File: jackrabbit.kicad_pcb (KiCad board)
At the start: 2 copper layers, 50 x 48.3 mm, 61 parts, among them J1 USB_C, J2 PinHeader_2.54mm_02x08, J3 PinHeader_2.54mm_02x08, J4 PinHeader_2.54mm_02x04, J5 PinHeader_2.54mm_02x04, J6 PinHeader_2.54mm_01x04, J7 PinHeader_2.54mm_01x03, SW1 SW_Push, SW2 SW_Push, U1 MIC5319-3.3YD5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

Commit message: Add pullups to disable buffers on power-on
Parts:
- added R18: 10k, Resistor_SMD:R_0603_1608Metric_Pad0.98x0.95mm_HandSolder, F.Cu at (115.6, 94.0)
- added R19: 10k, Resistor_SMD:R_0603_1608Metric_Pad0.98x0.95mm_HandSolder, F.Cu at (115.6, 96.5)
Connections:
- U2 pad 19: GND -> /~{OE_A}
- U4 pad 31: unconnected-(U4-Pad31) -> /~{OE_A}
- U4 pad 32: unconnected-(U4-Pad32) -> /~{OE_B}
- U5 pad 19: GND -> /~{OE_B}
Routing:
- net /QSPI_SD3: track 20.6 -> 22.2 mm
- net /QSPI_SD1: track 8.21 -> 6.62 mm
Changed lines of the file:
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@@
   (title_block
     (title "Jackrabbit RP2040 Logic Analyzer")
-    (date "2022-07-10")
+    (date "2022-07-21")
     (rev "A")
     (comment 2 "Ray Sun")
@@
   (net 74 "/DIG14")
   (net 75 "/DIG15")
-  (net 76 "unconnected-(U4-Pad32)")
+  (net 76 "/~{OE_A}")
   (net 77 "unconnected-(U4-Pad34)")
-  (net 78 "unconnected-(U4-Pad31)")
+  (net 78 "/~{OE_B}")
   (net 79 "Net-(R7-Pad1)")
   (net 80 "Net-(R8-Pad1)")
@@
       (net 80 "Net-(R8-Pad1)") (pinfunction "GPIO19") (pintype "bidirectional"))
     (pad "31" smd roundrect (at 3.65 1.8 315) (size 1.3 0.2) (layers "F.Cu" "F.Paste" "F.Mask") (roundrect_rratio 0.25)
-      (net 78 "unconnected-(U4-Pad31)") (pinfunction "GPIO20") (pintype "bidirectional+no_connect"))
+      (net 76 "/~{OE_A}") (pinfunction "GPIO20") (pintype "bidirectional"))
     (pad "32" smd roundrect (at 3.65 1.4 315) (size 1.3 0.2) (layers "F.Cu" "F.Paste" "F.Mask") (roundrect_rratio 0.25)
-      (net 76 "unconnected-(U4-Pad32)") (pinfunction "GPIO21") (pintype "bidirectional+no_connect"))
+      (net 78 "/~{OE_B}") (pinfunction "GPIO21") (pintype "bidirectional"))
     (pad "33" smd roundrect (at 3.65 1 315) (size 1.3 0.2) (layers "F.Cu" "F.Paste" "F.Mask") (roundrect_rratio 0.25)
       (net 1 "+3V3") (pinfunction "IOVDD") (pintype "power_in"))
@@
       (net 89 "Net-(RN2-Pad1)") (pinfunction "B0") (pintype "tri_state"))
     (pad "19" smd roundrect (at 2.8625 -1.75 90) (size 1.475 0.3) (layers "F.Cu" "F.Paste" "F.Mask") (roundrect_rratio 0.25)
-      (net 2 "GND") (pinfunction "CE") (pintype "input"))
+      (net 78 "/~{OE_B}") (pinfunction "CE") (pintype "input"))
     (pad "20" smd roundrect (at 2.8625 -2.25 90) (size 1.475 0.3) (layers "F.Cu" "F.Paste" "F.Mask") (roundrect_rratio 0.25)
       (net 1 "+3V3") (pinfunction "VCC") (pintype "power_in"))
@@
     )
   )
+  (footprint "Resistor_SMD:R_0603_1608Metric_Pad0.98x0.95mm_HandSolder" (layer "F.Cu")
+    (at 115.632 96.475)
+    (descr "Resistor SMD 0603 (1608 Metric), square (rectangular) end terminal, IPC_7351 nominal with elongated pad for handsoldering. (Body size source: IPC-SM-782 page 72, https://www.pcb-3d.com/wordpress/wp-content/uploads/ipc-sm-782a_amendment_1_and_2.pdf), generated with kicad-footprint-generator")
+    (tags "resistor handsolder")
+    (property "Sheetfile" "jackrabbit.kicad_sch")
+    (property "Sheetname" "")
+    (attr smd)
+    (fp_text reference "R19" (at 0 -1.429992 unlocked) (layer "F.SilkS") hide
+      (effects (font (size 0.762 0.762) (thickness 0.127)))
+    )
+    (fp_text value "10k" (at 0 1.43 unlocked) (layer "F.Fab")
+      (effects (font (size 0.762 0.762) (thickness 0.127)))
+    )
+    (fp_text user "${REFERENCE}" (at 0 0 unlocked) (layer "F.Fab")
+      (effects (font (size 0.762 0.762) (thickness 0.127)))
+    )
+    (fp_line (start -0.254724 -0.5225) (end 0.254724 -0.5225) (layer "F.SilkS") (width 0.12))
+    (fp_line (start -0.254724 0.5225) (end 0.254724 0.5225) (layer "F.SilkS") (width 0.12))
+    (fp_line (start -1.65 0.73) (end -1.65 -0.73) (layer "F.CrtYd") (width 0.05))
+    (fp_line (start 1.65 0.73) (end -1.65 0.73) (layer "F.CrtYd") (width 0.05))
+    (fp_line (start 1.65 -0.73) (end 1.65 0.73) (layer "F.CrtYd") (width 0.05))
+    (fp_line (start -1.65 -0.73) (end 1.65 -0.73) (layer "F.CrtYd") (width 0.05))
+    (fp_line (start 0.8 0.4125) (end -0.8 0.4125) (layer "F.Fab") (width 0.1))
+    (fp_line (start 0.8 -0.4125) (end 0.8 0.4125) (layer "F.Fab") (width 0.1))
+    (fp_line (start -0.8 -0.4125) (end 0.8 -0.4125) (layer "F.Fab") (width 0.1))
+    (fp_line (start -0.8 0.4125) (end -0.8 -0.4125) (layer "F.Fab") (width 0.1))
+    (pad "1" smd roundrect (at -0.9125 0) (size 0.975 0.95) (layers "F.Cu" "F.Paste" "F.Mask") (roundrect_rratio 0.25)
+      (net 1 "+3V3") (pintype "passive"))
+    (pad "2" smd roundrect (at 0.9125 0) (size 0.975 0.95) (layers "F.Cu" "F.Paste" "F.Mask") (roundrect_rratio 0.25)
+      (net 78 "/~{OE_B}") (pintype "passive"))
+    (model "${KICAD6_3DMODEL_DIR}/Resistor_SMD.3dshapes/R_0603_1608Metric.wrl"
+      (offset (xyz 0 0 0))
+      (scale (xyz 1 1 1))
+      (rotate (xyz 0 0 0))
+    )
+  )
   (footprint "Connector_PinHeader_2.54mm:PinHeader_1x04_P2.54mm_Vertical" (layer "F.Cu")
     (at 142.81 140.955 90)
@@
   )
   (footprint "Resistor_SMD:R_0603_1608Metric_Pad0.98x0.95mm_HandSolder" (layer "F.Cu")
+    (at 115.632 93.965)
+    (descr "Resistor SMD 0603 (1608 Metric), square (rectangular) end terminal, IPC_7351 nominal with elongated pad for handsoldering. (Body size source: IPC-SM-782 page 72, https://www.pcb-3d.com/wordpress/wp-content/uploads/ipc-sm-782a_amendment_1_and_2.pdf), generated with kicad-footprint-generator")
+    (tags "resistor handsolder")
+    (property "Sheetfile" "jackrabbit.kicad_sch")
+    (property "Sheetname" "")
+    (attr smd)
+    (fp_text reference "R18" (at 0 -1.429995 unlocked) (layer "F.SilkS") hide
+      (effects (font (size 0.762 0.762) (thickness 0.127)))
+    )
+    (fp_text value "10k" (at 0 1.43 unlocked) (layer "F.Fab")
+      (effects (font (size 0.762 0.762) (thickness 0.127)))
+    )
+    (fp_text user "${REFERENCE}" (at 0 0 unlocked) (layer "F.Fab")
+      (effects (font (size 0.762 0.762) (thickness 0.127)))
+    )
+    (fp_line (start -0.254724 0.5225) (end 0.254724 0.5225) (layer "F.SilkS") (width 0.12))
+    (fp_line (start -0.254724 -0.5225) (end 0.254724 -0.5225) (layer "F.SilkS") (width 0.12))
+    (fp_line (start -1.65 0.73) (end -1.65 -0.73) (layer "F.CrtYd") (width 0.05))
+    (fp_line (start 1.65 -0.73) (end 1.65 0.73) (layer "F.CrtYd") (width 0.05))
+    (fp_line (start 1.65 0.73) (end -1.65 0.73) (layer "F.CrtYd") (width 0.05))
+    (fp_line (start -1.65 -0.73) (end 1.65 -0.73) (layer "F.CrtYd") (width 0.05))
+    (fp_line (start -0.8 -0.4125) (end 0.8 -0.4125) (layer "F.Fab") (width 0.1))
+    (fp_line (start -0.8 0.4125) (end -0.8 -0.4125) (layer "F.Fab") (width 0.1))
+    (fp_line (start 0.8 -0.4125) (end 0.8 0.4125) (layer "F.Fab") (width 0.1))
+    (fp_line (start 0.8 0.4125) (end -0.8 0.4125) (layer "F.Fab") (width 0.1))
+    (pad "1" smd roundrect (at -0.9125 0) (size 0.975 0.95) (layers "F.Cu" "F.Paste" "F.Mask") (roundrect_rratio 0.25)
+      (net 1 "+3V3") (pintype "passive"))
+    (pad "2" smd roundrect (at 0.9125 0) (size 0.975 0.95) (layers "F.Cu" "F.Paste" "F.Mask") (roundrect_rratio 0.25)
+      (net 76 "/~{OE_A}") (pintype "passive"))
+    (model "${KICAD6_3DMODEL_DIR}/Resistor_SMD.3dshapes/R_0603_1608Metric.wrl"
+      (offset (xyz 0 0 0))
+      (scale (xyz 1 1 1))
+      (rotate (xyz 0 0 0))
+    )
+  )
+  (footprint "Resistor_SMD:R_0603_1608Metric_Pad0.98x0.95mm_HandSolder" (layer "F.Cu")
     (at 154.494 127.493 90)
     (descr "Resistor SMD 0603 (1608 Metric), square (rectangular) end terminal, IPC_7351 nominal with elongated pad for handsoldering. (Body size source: IPC-SM-782 page 72, https://www.pcb-3d.com/wordpress/wp-content/uploads/ipc-sm-782a_amendment_1_and_2.pdf), generated with kicad-footprint-generator")
@@
       (net 81 "Net-(RN1-Pad1)") (pinfunction "B0") (pintype "tri_state"))
     (pad "19" smd roundrect (at 2.8625 -1.75 270) (size 1.475 0.3) (layers "F.Cu" "F.Paste" "F.Mask") (roundrect_rratio 0.25)
-      (net 2 "GND") (pinfunction "CE") (pintype "input"))
+      (net 76 "/~{OE_A}") (pinfunction "CE") (pintype "input"))
     (pad "20" smd roundrect (at 2.8625 -2.25 270) (size 1.475 0.3) (layers "F.Cu" "F.Paste" "F.Mask") (roundrect_rratio 0.25)
       (net 1 "+3V3") (pinfunction "VCC") (pintype "power_in"))
@@
   (segment (start 142.429 115.047) (end 141.54 114.158) (width 0.2032) (layer "F.Cu") (net 63))
   (segment (start 141.54 114.158) (end 139.508 114.158) (width 0.2032) (layer "F.Cu") (net 63))
-  (segment (start 142.937 113.015) (end 142.937 111.426) (width 0.2032) (layer "F.Cu") (net 63))
   (segment (start 142.429 115.87273) (end 142.429 115.047) (width 0.2032) (layer "F.Cu") (net 63))
   (segment (start 142.81 114.793) (end 141.667 113.65) (width 0.2032) (layer "F.Cu") (net 64))
@@
   (segment (start 147.636 113.015) (end 147.636 104.887) (width 0.2032) (layer "F.Cu") (net 67))
   (segment (start 146.747 103.998) (end 144.207 103.998) (width 0.2032) (layer "F.Cu") (net 67))
+  (segment (start 142.937 113.015) (end 142.937 111.426) (width 0.2032) (layer "F.Cu") (net 67))
   (segment (start 144.334 116.230472) (end 144.334 114.285) (width 0.2032) (layer "F.Cu") (net 67))
   (segment (start 142.934676 117.629796) (end 144.334 116.230472) (width 0.2032) (layer "F.Cu") (net 67))

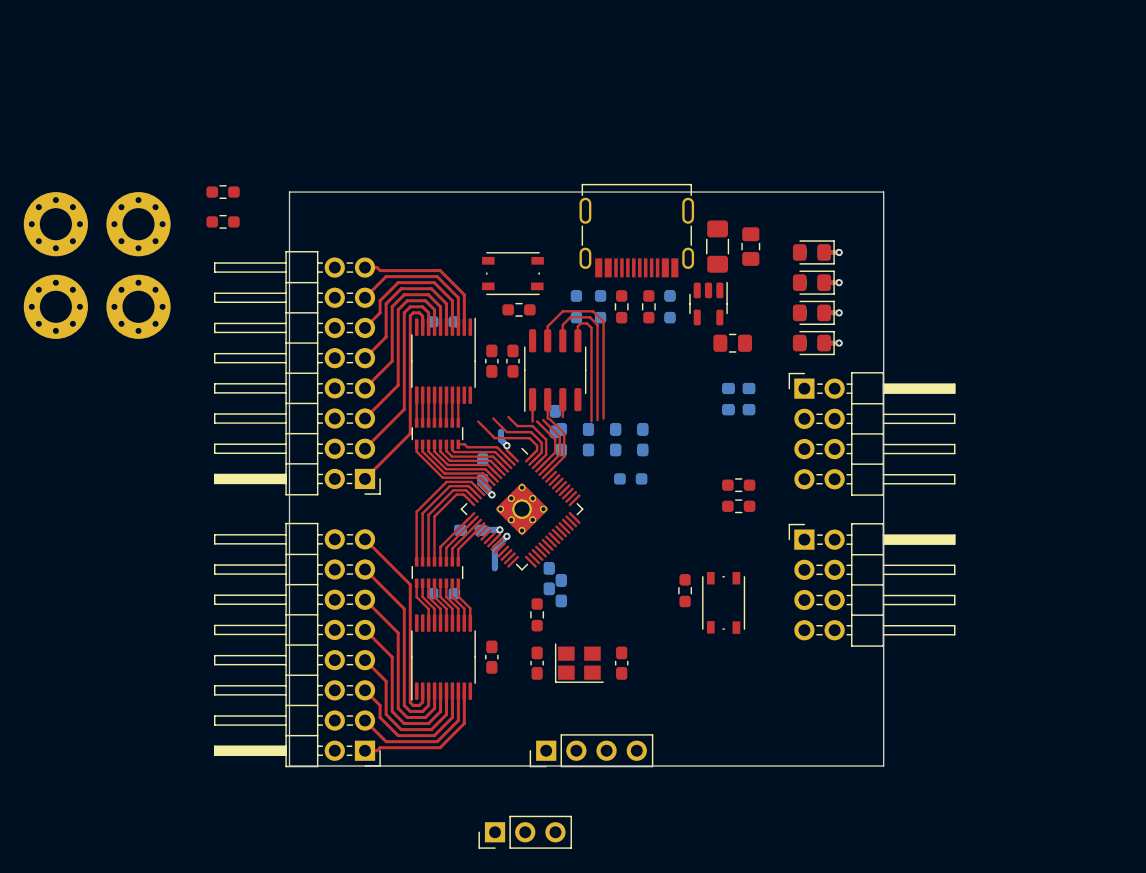
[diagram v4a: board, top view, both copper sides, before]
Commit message: Redo placement to put USB and digital connector on long axis
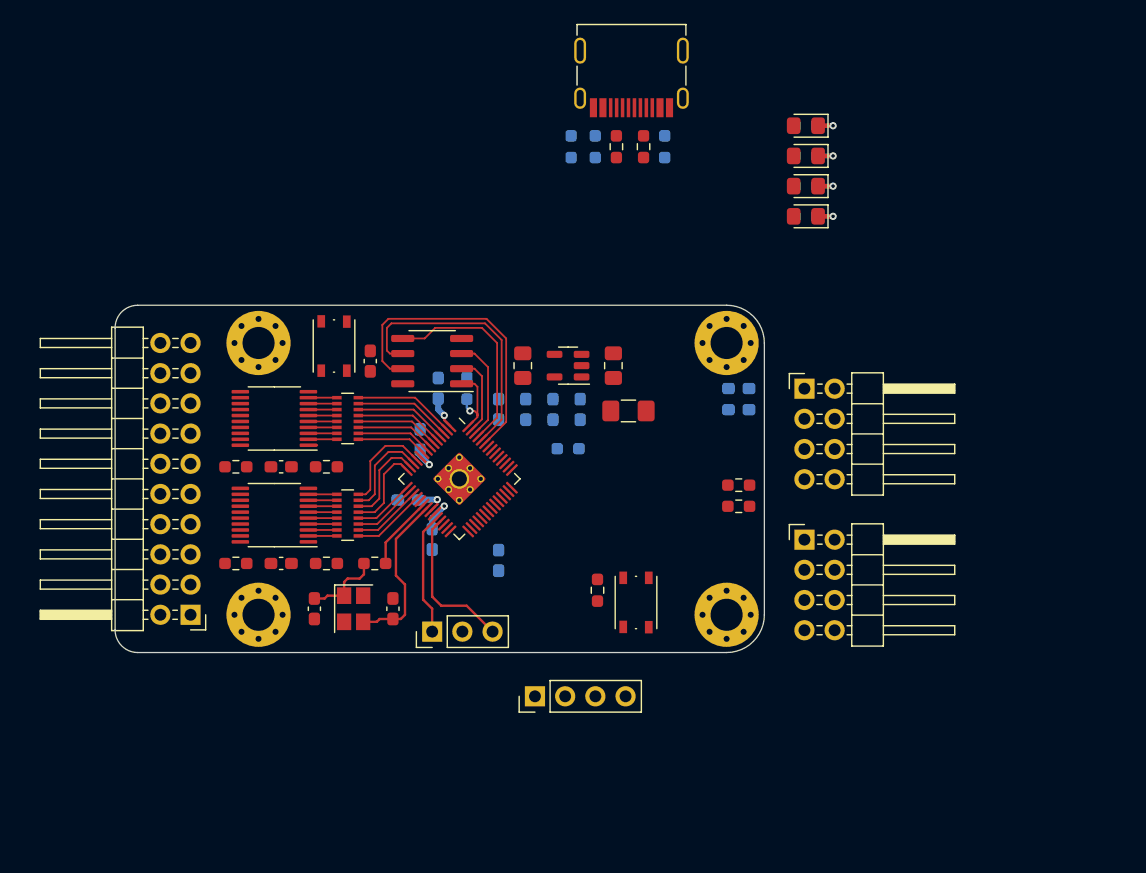
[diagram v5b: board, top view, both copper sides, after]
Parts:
- removed the J3 at (127.6, 141.0)
- J2: value PinHeader_2.54mm_02x08 -> PinHeader_2.54mm_02x10; footprint Connector_PinHeader_2.54mm:PinHeader_2x08_P2.54mm_Horizontal -> Connector_PinHeader_2.54mm:PinHeader_2x10_P2.54mm_Horizontal
- R12, R9: moved to F.Cu
- R6: moved to B.Cu
- moved H1 55.8 mm to (158.0, 129.5)
- moved H3 50.5 mm to (158.0, 106.7)
- moved H4 31.0 mm to (118.6, 129.5)
- moved R19 28.7 mm to (116.7, 125.2), turned to 180 degrees
- moved R18 23.1 mm to (116.7, 117.1), turned to 180 degrees
- moved C11 19.8 mm to (120.5, 117.1), turned to 0 degrees
- moved C18 19.8 mm to (129.9, 129.0), turned to -90 degrees
- moved H2 19.8 mm to (118.6, 106.7)
- moved Y1 19.5 mm to (126.6, 129.0), turned to -90 degrees
- moved C16 19.4 mm to (120.5, 125.2), turned to 0 degrees
- moved C17 19.3 mm to (123.3, 129.0), turned to 90 degrees
- moved J2 18.6 mm to (112.9, 129.5)
- moved U5 18.6 mm to (119.9, 121.1), turned to 180 degrees
- moved C3 17.8 mm to (140.8, 108.6), turned to 90 degrees
- moved J6 17.7 mm to (133.2, 130.9)
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- renumbered J4 to J3, J5 to J4, J6 to J5, J7 to J6
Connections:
- J2 pad 1: /OUT_DIG7 -> GND
- J2 pad 10: GND -> /OUT_DIG9
- J2 pad 11: /OUT_DIG2 -> /OUT_DIG6
- J2 pad 12: GND -> /OUT_DIG7
- J2 pad 13: /OUT_DIG1 -> /OUT_DIG4
- J2 pad 14: GND -> /OUT_DIG5
- J2 pad 15: /OUT_DIG0 -> /OUT_DIG2
- J2 pad 16: GND -> /OUT_DIG3
- J2 pad 3: /OUT_DIG6 -> /OUT_DIG14
- J2 pad 4: GND -> /OUT_DIG15
- J2 pad 5: /OUT_DIG5 -> /OUT_DIG12
- J2 pad 6: GND -> /OUT_DIG13
- J2 pad 7: /OUT_DIG4 -> /OUT_DIG10
- J2 pad 8: GND -> /OUT_DIG11
- J2 pad 9: /OUT_DIG3 -> /OUT_DIG8
- J3 pad 7: /ADC0 -> unconnected-(J3-Pad7)
- R12 pad 2: GND -> +3V3
- R9 pad 2: GND -> +3V3
- RN1 pad 1: Net-(RN1-Pad1) -> /DIG7
- RN1 pad 10: /DIG6 -> Net-(RN1-Pad10)
- RN1 pad 11: /DIG5 -> Net-(RN1-Pad11)
- RN1 pad 12: /DIG4 -> Net-(RN1-Pad12)
- RN1 pad 13: /DIG3 -> Net-(RN1-Pad13)
- RN1 pad 14: /DIG2 -> Net-(RN1-Pad14)
- RN1 pad 15: /DIG1 -> Net-(RN1-Pad15)
- RN1 pad 16: /DIG0 -> Net-(RN1-Pad16)
- RN1 pad 2: Net-(RN1-Pad2) -> /DIG6
- RN1 pad 3: Net-(RN1-Pad3) -> /DIG5
- RN1 pad 4: Net-(RN1-Pad4) -> /DIG4
- RN1 pad 5: Net-(RN1-Pad5) -> /DIG3
- RN1 pad 6: Net-(RN1-Pad6) -> /DIG2
- RN1 pad 7: Net-(RN1-Pad7) -> /DIG1
- RN1 pad 8: Net-(RN1-Pad8) -> /DIG0
- RN1 pad 9: /DIG7 -> Net-(RN1-Pad9)
- RN2 pad 1: Net-(RN2-Pad1) -> /DIG15
- RN2 pad 10: /DIG14 -> Net-(RN2-Pad10)
- RN2 pad 11: /DIG13 -> Net-(RN2-Pad11)
- RN2 pad 12: /DIG12 -> Net-(RN2-Pad12)
- RN2 pad 13: /DIG11 -> Net-(RN2-Pad13)
- RN2 pad 14: /DIG10 -> Net-(RN2-Pad14)
- RN2 pad 15: /DIG9 -> Net-(RN2-Pad15)
- RN2 pad 16: /DIG8 -> Net-(RN2-Pad16)
- RN2 pad 2: Net-(RN2-Pad2) -> /DIG14
- RN2 pad 3: Net-(RN2-Pad3) -> /DIG13
- RN2 pad 4: Net-(RN2-Pad4) -> /DIG12
- RN2 pad 5: Net-(RN2-Pad5) -> /DIG11
- RN2 pad 6: Net-(RN2-Pad6) -> /DIG10
- RN2 pad 7: Net-(RN2-Pad7) -> /DIG9
- RN2 pad 8: Net-(RN2-Pad8) -> /DIG8
- RN2 pad 9: /DIG15 -> Net-(RN2-Pad9)
- U2 pad 11: Net-(RN1-Pad8) -> /OUT_DIG0
- U2 pad 12: Net-(RN1-Pad7) -> /OUT_DIG1
- U2 pad 13: Net-(RN1-Pad6) -> /OUT_DIG2
- U2 pad 14: Net-(RN1-Pad5) -> /OUT_DIG3
- U2 pad 15: Net-(RN1-Pad4) -> /OUT_DIG4
- U2 pad 16: Net-(RN1-Pad3) -> /OUT_DIG5
- U2 pad 17: Net-(RN1-Pad2) -> /OUT_DIG6
- U2 pad 18: Net-(RN1-Pad1) -> /OUT_DIG7
- U2 pad 2: /OUT_DIG0 -> Net-(RN1-Pad16)
- U2 pad 3: /OUT_DIG1 -> Net-(RN1-Pad15)
- U2 pad 4: /OUT_DIG2 -> Net-(RN1-Pad14)
- U2 pad 5: /OUT_DIG3 -> Net-(RN1-Pad13)
- U2 pad 6: /OUT_DIG4 -> Net-(RN1-Pad12)
- U2 pad 7: /OUT_DIG5 -> Net-(RN1-Pad11)
- U2 pad 8: /OUT_DIG6 -> Net-(RN1-Pad10)
- U2 pad 9: /OUT_DIG7 -> Net-(RN1-Pad9)
- U5 pad 11: Net-(RN2-Pad8) -> /OUT_DIG8
- U5 pad 12: Net-(RN2-Pad7) -> /OUT_DIG9
- U5 pad 13: Net-(RN2-Pad6) -> /OUT_DIG10
- U5 pad 14: Net-(RN2-Pad5) -> /OUT_DIG11
- U5 pad 15: Net-(RN2-Pad4) -> /OUT_DIG12
- U5 pad 16: Net-(RN2-Pad3) -> /OUT_DIG13
- U5 pad 17: Net-(RN2-Pad2) -> /OUT_DIG14
- U5 pad 18: Net-(RN2-Pad1) -> /OUT_DIG15
- U5 pad 2: /OUT_DIG8 -> Net-(RN2-Pad16)
- U5 pad 3: /OUT_DIG9 -> Net-(RN2-Pad15)
- U5 pad 4: /OUT_DIG10 -> Net-(RN2-Pad14)
- U5 pad 5: /OUT_DIG11 -> Net-(RN2-Pad13)
- U5 pad 6: /OUT_DIG12 -> Net-(RN2-Pad12)
- U5 pad 7: /OUT_DIG13 -> Net-(RN2-Pad11)
- U5 pad 8: /OUT_DIG14 -> Net-(RN2-Pad10)
- U5 pad 9: /OUT_DIG15 -> Net-(RN2-Pad9)
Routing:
- net /OUT_DIG8: track 17.5 -> 0.00 mm
- net /OUT_DIG7: track 17.5 -> 0.00 mm
- net /OUT_DIG6: track 16.5 -> 0.00 mm
- net /OUT_DIG9: track 16.5 -> 0.00 mm
- net /OUT_DIG5: track 15.4 -> 0.00 mm
- net /OUT_DIG10: track 15.4 -> 0.00 mm
- net /OUT_DIG11: track 14.4 -> 0.00 mm
- net /OUT_DIG4: track 14.4 -> 0.00 mm
- net Net-(C18-Pad2): track 0.00 -> 14.2 mm
- net /OUT_DIG3: track 13.4 -> 0.00 mm
- net /OUT_DIG12: track 13.4 -> 0.00 mm
- net /SWDIO: track 0.00 -> 12.9 mm
- net /OUT_DIG2: track 12.4 -> 0.00 mm
- net /OUT_DIG13: track 12.4 -> 0.00 mm
- net /OUT_DIG15: track 12.0 -> 0.00 mm
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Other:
- board size 50 x 48.3 mm -> 54.6 x 29.2 mm

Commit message: Change footprints to those of ordered parts
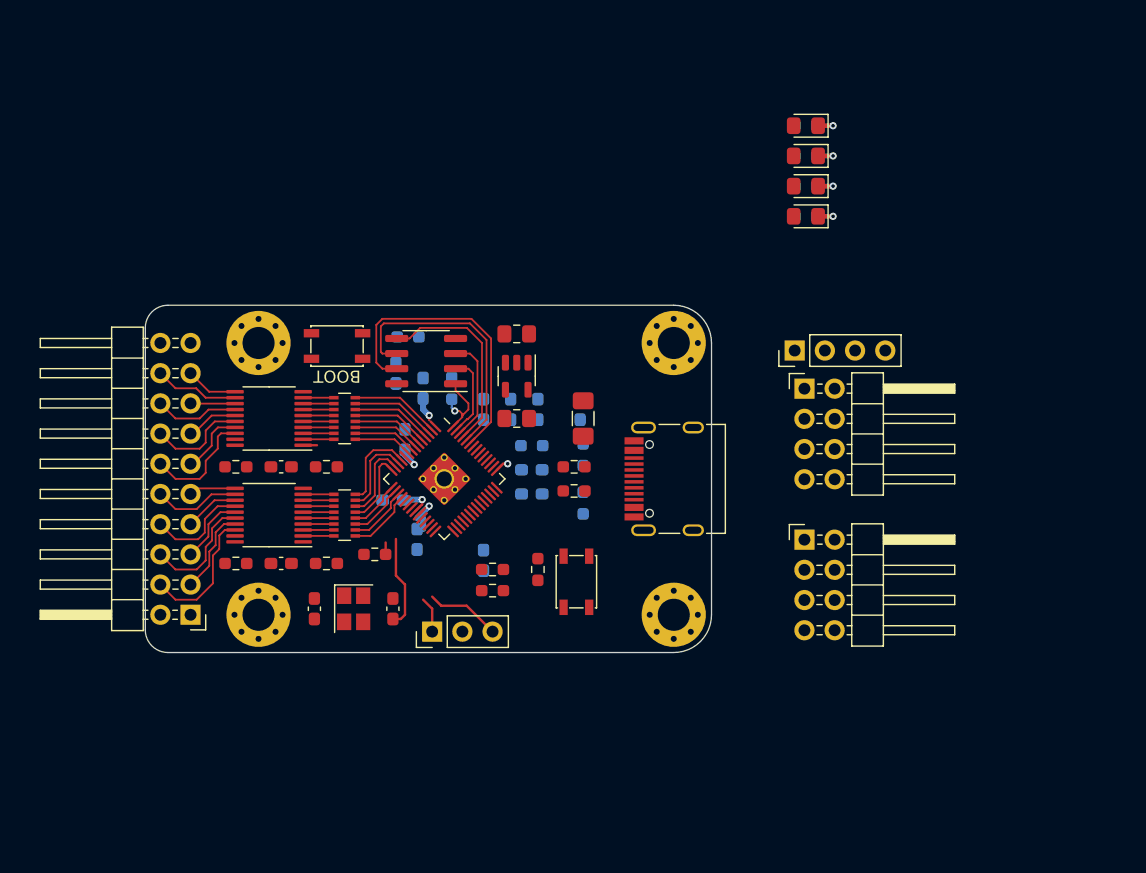
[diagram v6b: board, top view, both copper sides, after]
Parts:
- C15: moved to B.Cu
- J1: footprint jackrabbit:USB_C_Receptacle_Molex_2171790001 -> jackrabbit:USB_C_Receptacle_GCT_USB4105-GF-A-120
- SW1, SW2: footprint Button_Switch_SMD:SW_Push_1P1T_NO_Vertical_Wuerth_434133025816 -> jackrabbit:SW_Push_CK_PTS815_HandSoldering
- moved J5 36.4 mm to (163.7, 107.3)
- moved J1 32.0 mm to (151.0, 118.1), turned to 90 degrees
- moved R2 30.7 mm to (145.9, 120.1), turned to 90 degrees
- moved R5 29.5 mm to (145.2, 119.1), turned to 0 degrees
- moved R4 27.2 mm to (145.2, 117.1), turned to 0 degrees
- moved R1 25.9 mm to (145.9, 116.1)
- moved R7 21.9 mm to (138.3, 127.5)
- moved R8 21.9 mm to (138.3, 125.7)
- moved R10 21.1 mm to (131.2, 106.2), turned to 180 degrees
- moved C5 18.8 mm to (141.6, 119.4)
- moved C14 18.7 mm to (141.6, 117.3)
- moved C2 8.55 mm to (140.3, 105.9), turned to 180 degrees
- moved SW2 5.31 mm to (145.3, 126.7)
- moved R13 5.31 mm to (142.1, 125.7)
- moved C3 4.47 mm to (140.3, 113.0), turned to 180 degrees
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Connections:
- J1 pad S1: GND -> unconnected-(J1-PadS1)
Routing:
- net /OUT_DIG15: track 0.00 -> 11.3 mm
- net /OUT_DIG13: track 0.00 -> 9.86 mm
- net /OUT_DIG7: track 0.00 -> 9.58 mm
- net /OUT_DIG11: track 0.00 -> 8.63 mm
- net /OUT_DIG5: track 0.00 -> 8.35 mm
- net /SWCLK: track 10.4 -> 3.00 mm
- net /OUT_DIG9: track 0.00 -> 7.32 mm
- net /OUT_DIG14: track 0.00 -> 7.19 mm
- net /OUT_DIG1: track 0.00 -> 7.13 mm
- net /OUT_DIG3: track 0.00 -> 7.12 mm
- net /SWDIO: track 12.9 -> 6.30 mm
- net Net-(C17-Pad2): track 6.60 -> 0.00 mm
- net Net-(C18-Pad2): track 14.2 -> 7.86 mm
- net /OUT_DIG12: track 0.00 -> 5.82 mm
- net /OUT_DIG6: track 0.00 -> 5.60 mm
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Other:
- board size 54.6 x 29.2 mm -> 47.6 x 29.2 mm
- board text added: "BOOT"
